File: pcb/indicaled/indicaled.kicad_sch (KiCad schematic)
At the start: 17 parts

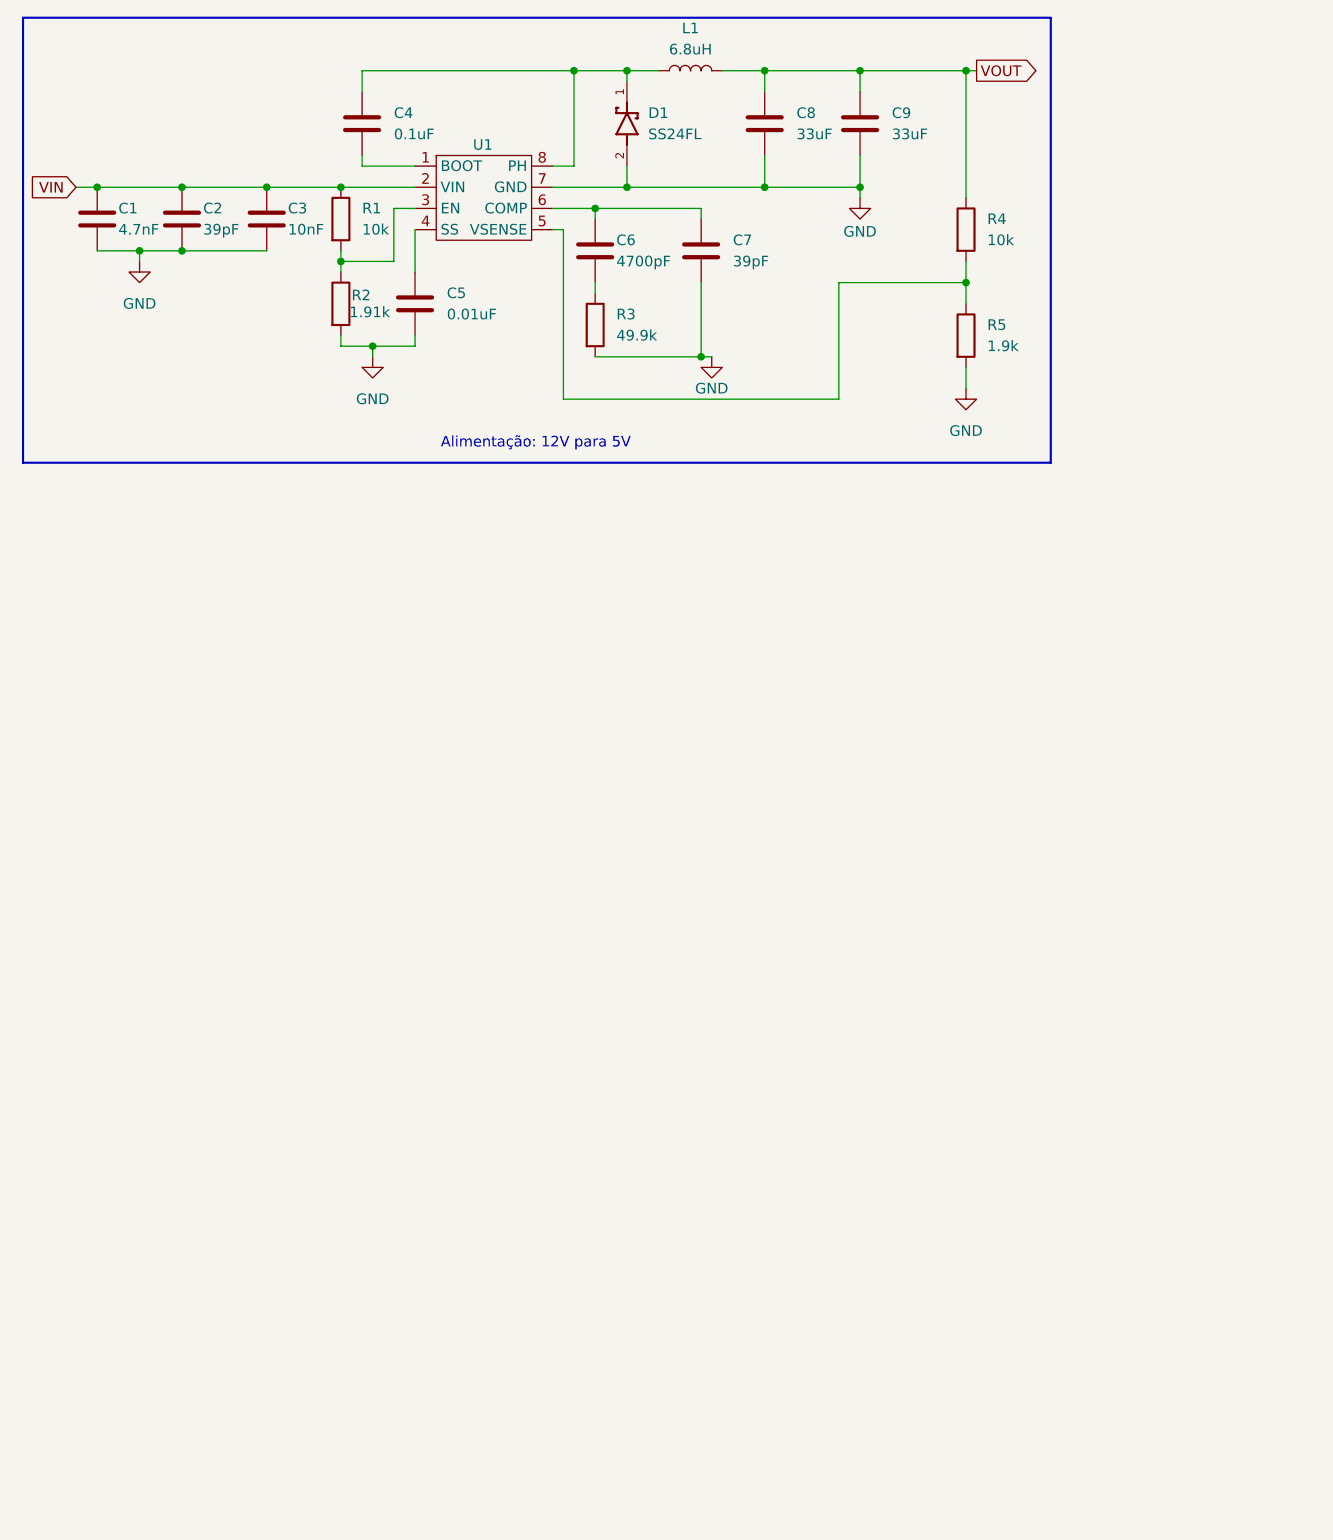
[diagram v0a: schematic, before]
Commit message: adicionando os transistores que vão retificar o sinal do caro pro ESP
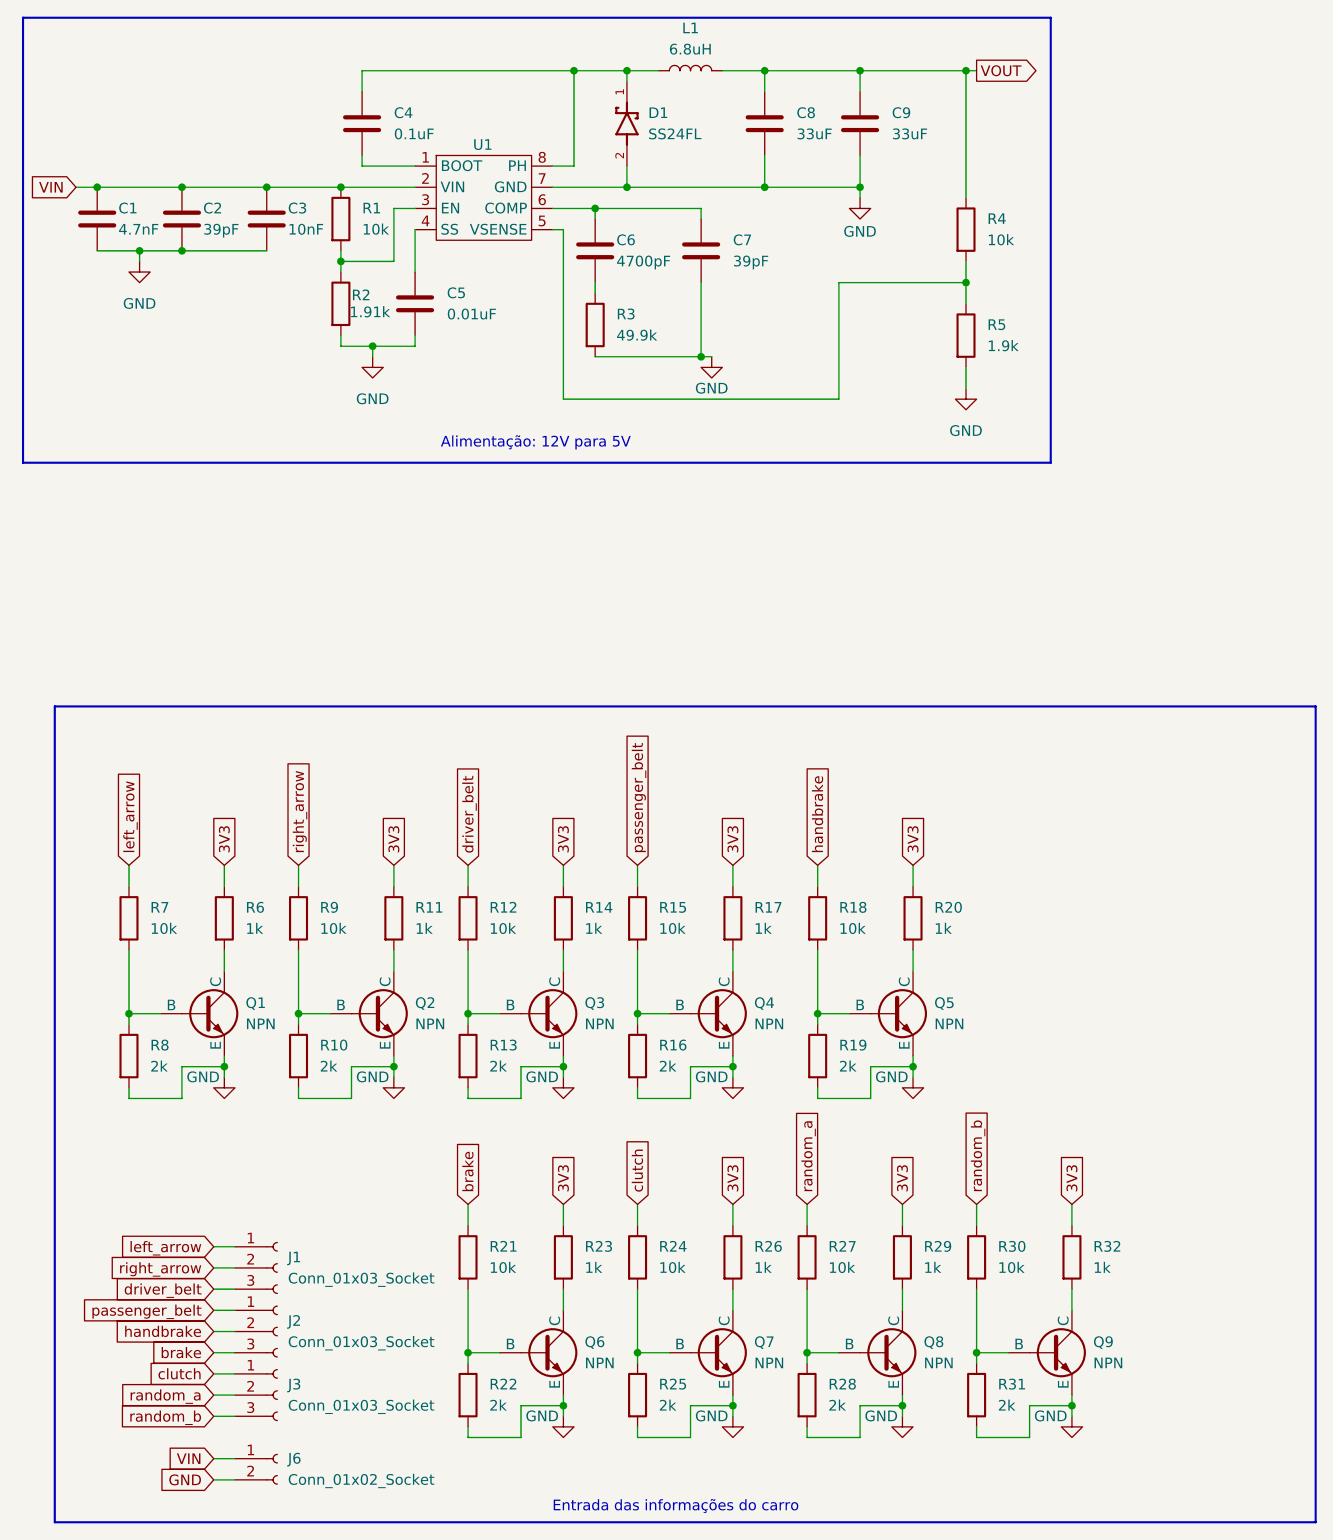
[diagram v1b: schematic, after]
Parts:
- added J1, J2, J3: Conn_01x03_Socket, symbol Connector:Conn_01x03_Socket
- added J6: Conn_01x02_Socket, symbol Connector:Conn_01x02_Socket
- added Q1, Q2, Q3, Q4, Q5, Q6, Q7, Q8, Q9: NPN, Package_TO_SOT_SMD:SOT-23, symbol Simulation_SPICE:NPN
- added R10, R13, R16, R19, R22, R25, R28, R31, R8: 2k, Resistor_SMD:R_0201_0603Metric, symbol Device:R
- added R11, R14, R17, R20, R23, R26, R29, R32, R6: 1k, Resistor_SMD:R_0201_0603Metric, symbol Device:R
- added R12, R15, R18, R21, R24, R27, R30, R7, R9: 10k, Resistor_SMD:R_0201_0603Metric, symbol Device:R
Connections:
- net GND: now also J6.2 (Pin_2), Q1.3 (E), Q2.3 (E), Q3.3 (E), Q4.3 (E), Q5.3 (E), Q6.3 (E), Q7.3 (E), Q8.3 (E), Q9.3 (E), R10.2, R13.2, R16.2, R19.2, R22.2, R25.2, R28.2, R31.2, R8.2
- net VIN: now also J6.1 (Pin_1)
- new net: Q2.1 (C), R11.2
- new net: Q2.2 (B), R10.1, R9.2
- new net: Q8.2 (B), R27.2, R28.1
- new net: Q3.2 (B), R12.2, R13.1
- new net: Q1.1 (C), R6.2
- new net: Q7.1 (C), R26.2
- new net: Q9.1 (C), R32.2
- new net: Q9.2 (B), R30.2, R31.1
- new net: Q1.2 (B), R7.2, R8.1
- new net: Q7.2 (B), R24.2, R25.1
- new net: Q6.2 (B), R21.2, R22.1
- new net: Q4.1 (C), R17.2
- new net: Q5.1 (C), R20.2
- new net: Q5.2 (B), R18.2, R19.1
- new net: Q6.1 (C), R23.2
- new net: Q4.2 (B), R15.2, R16.1
- new net: Q3.1 (C), R14.2
- new net: Q8.1 (C), R29.2
- new net 3V3: R11.1, R14.1, R17.1, R20.1, R23.1, R26.1, R29.1, R32.1, R6.1
- new net brake: J2.3 (Pin_3), R21.1
- new net clutch: J3.1 (Pin_1), R24.1
- new net driver_belt: J1.3 (Pin_3), R12.1
- new net handbrake: J2.2 (Pin_2), R18.1
- new net left_arrow: J1.1 (Pin_1), R7.1
- new net passenger_belt: J2.1 (Pin_1), R15.1
- new net random_a: J3.2 (Pin_2), R27.1
- new net random_b: J3.3 (Pin_3), R30.1
- new net right_arrow: J1.2 (Pin_2), R9.1
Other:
- note added: "Entrada das informações do carro"
